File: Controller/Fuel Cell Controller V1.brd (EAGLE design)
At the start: 160 x 100 mm, 131 parts, among them IC1 4081D, M1 MOSFETBOARD, T1 TEENSY_3.1_ALL_PINS, U1 SN74ALS153D, U2 MAX3221CPWR, U3 ATMEGA328P_TQFP, U4 ATMEGA328P_TQFP, U5 MAX3221CPWR, U6 ATMEGA328P_TQFP

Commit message: added gerbers
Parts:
- removed U$1: TRUMP, trump:TRUMP
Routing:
- net SDA: track 242.7 -> 241.0 mm
- net SCL: track 237.0 -> 236.1 mm
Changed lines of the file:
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@@
 <setting verticaltext="up"/>
 </settings>
-<grid distance="0.003125" unitdist="inch" unit="inch" style="lines" multiple="1" display="no" altdistance="0.025" altunitdist="inch" altunit="inch"/>
+<grid distance="0.003125" unitdist="inch" unit="mil" style="lines" multiple="1" display="no" altdistance="0.025" altunitdist="inch" altunit="inch"/>
 <layers>
 <layer number="1" name="Top" color="4" fill="1" visible="yes" active="yes"/>
@@
 <attribute name="VALUE" x="80.0735" y="91.424125" size="0.7" layer="22" ratio="15" rot="MR180"/>
 </element>
-<element name="U$1" library="trump" package="TRUMP" value="TRUMP" x="148.11375" y="64.849375" rot="MR0"/>
 </elements>
 <signals>
@@
 <wire x1="67.31" y1="70.485" x2="67.31" y2="72.39" width="0.4064" layer="16"/>
 <via x="67.31" y="72.39" extent="1-16" drill="0.6"/>
-<wire x1="78.74" y1="52.07" x2="81.28" y2="49.53" width="0.4064" layer="1"/>
-<wire x1="81.28" y1="49.53" x2="138.1125" y2="49.53" width="0.4064" layer="1"/>
-<wire x1="138.1125" y1="49.53" x2="152.7175" y2="34.925" width="0.4064" layer="1"/>
-<wire x1="152.7175" y1="34.925" x2="152.7175" y2="32.0675" width="0.4064" layer="1"/>
-<wire x1="152.7175" y1="32.0675" x2="156.845" y2="27.94" width="0.4064" layer="1"/>
+<wire x1="78.74" y1="52.07" x2="81.12125" y2="49.68875" width="0.4064" layer="1"/>
+<wire x1="81.12125" y1="49.68875" x2="81.28" y2="49.53" width="0.4064" layer="1"/>
 <wire x1="40.1574" y1="36.76" x2="38.805" y2="36.76" width="0.4064" layer="1"/>
 <wire x1="38.805" y1="36.76" x2="37.4253125" y2="38.1396875" width="0.4064" layer="1"/>
@@
 <wire x1="37.62375" y1="38.735" x2="37.62375" y2="38.338125" width="0.4064" layer="1"/>
 <wire x1="37.62375" y1="38.338125" x2="37.4253125" y2="38.1396875" width="0.4064" layer="1"/>
+<wire x1="156.845" y1="27.94" x2="149.86" y2="27.94" width="0.4064" layer="1"/>
+<wire x1="149.86" y1="27.94" x2="128.349375" y2="49.450625" width="0.4064" layer="1"/>
+<wire x1="128.349375" y1="49.450625" x2="81.359375" y2="49.450625" width="0.4064" layer="1"/>
+<wire x1="81.359375" y1="49.450625" x2="81.28" y2="49.53" width="0.4064" layer="1"/>
 </signal>
 <signal name="SCL">
@@
 <wire x1="68.58" y1="65.405" x2="68.58" y2="71.4375" width="0.4064" layer="1"/>
 <wire x1="81.28" y1="52.07" x2="82.8675" y2="50.4825" width="0.4064" layer="1"/>
-<wire x1="82.8675" y1="50.4825" x2="138.43" y2="50.4825" width="0.4064" layer="1"/>
-<wire x1="138.43" y1="50.4825" x2="153.67" y2="35.2425" width="0.4064" layer="1"/>
-<wire x1="153.67" y1="35.2425" x2="153.67" y2="33.655" width="0.4064" layer="1"/>
-<wire x1="153.67" y1="33.655" x2="156.845" y2="30.48" width="0.4064" layer="1"/>
 <wire x1="40.1574" y1="35.96" x2="38.6525" y2="35.96" width="0.4064" layer="1"/>
 <wire x1="38.6525" y1="35.96" x2="37.7428125" y2="36.8696875" width="0.4064" layer="1"/>
@@
 <wire x1="37.62375" y1="30.00375" x2="37.62375" y2="36.750625" width="0.4064" layer="1"/>
 <wire x1="37.62375" y1="36.750625" x2="37.7428125" y2="36.8696875" width="0.4064" layer="1"/>
+<wire x1="82.8675" y1="50.4825" x2="131.365625" y2="50.4825" width="0.4064" layer="1"/>
+<wire x1="131.365625" y1="50.4825" x2="150.891875" y2="30.95625" width="0.4064" layer="1"/>
+<wire x1="150.891875" y1="30.95625" x2="156.36875" y2="30.95625" width="0.4064" layer="1"/>
+<wire x1="156.36875" y1="30.95625" x2="156.845" y2="30.48" width="0.4064" layer="1"/>
 </signal>
 <signal name="+3.3V">
@@
 <wire x1="32.7025" y1="28.865625" x2="34.051875" y2="28.865625" width="0.4064" layer="1"/>
 <wire x1="34.051875" y1="28.865625" x2="34.528125" y2="29.341875" width="0.4064" layer="1"/>
-<via x="25.24125" y="29.5275" extent="1-16" drill="0.6"/>
+<via x="25.24125" y="29.5275" extent="1-16" drill="0.5"/>
 <via x="25.55875" y="24.13" extent="1-16" drill="0.6"/>
 <via x="34.29" y="26.114375" extent="1-16" drill="0.6"/>
@@
 <wire x1="40.9575" y1="86.51875" x2="40.9575" y2="85.88375" width="1.27" layer="16"/>
 <wire x1="40.9575" y1="85.88375" x2="42.465625" y2="84.375625" width="1.778" layer="16"/>
-<wire x1="42.465625" y1="84.375625" x2="50.64125" y2="84.375625" width="1.778" layer="16"/>
-<wire x1="50.64125" y1="84.375625" x2="55.006875" y2="80.01" width="1.778" layer="16"/>
-<wire x1="55.006875" y1="80.01" x2="55.006875" y2="63.97625" width="1.778" layer="16"/>
-<wire x1="55.006875" y1="63.97625" x2="70.246875" y2="48.73625" width="1.778" layer="16"/>
-<wire x1="70.246875" y1="48.73625" x2="97.710625" y2="48.73625" width="1.778" layer="16"/>
-<wire x1="97.710625" y1="48.73625" x2="107.15625" y2="39.290625" width="1.778" layer="16"/>
+<wire x1="42.465625" y1="84.375625" x2="50.64125" y2="84.375625" width="2.1844" layer="16"/>
+<wire x1="50.64125" y1="84.375625" x2="55.006875" y2="80.01" width="2.1844" layer="16"/>
+<wire x1="55.006875" y1="80.01" x2="55.006875" y2="63.97625" width="2.1844" layer="16"/>
+<wire x1="55.006875" y1="63.97625" x2="70.246875" y2="48.73625" width="2.1844" layer="16"/>
+<wire x1="70.246875" y1="48.73625" x2="97.710625" y2="48.73625" width="2.1844" layer="16"/>
+<wire x1="97.710625" y1="48.73625" x2="107.15625" y2="39.290625" width="2.1844" layer="16"/>
 <polygon width="0.4064" layer="1" rank="2">
 <vertex x="75.565" y="-0.15875"/>
@@
 <vertex x="75.485625" y="11.7475"/>
 </polygon>
-<wire x1="107.15625" y1="39.290625" x2="107.15625" y2="32.146875" width="1.778" layer="16"/>
-<wire x1="107.15625" y1="30.1625" x2="107.15625" y2="3.33375" width="1.778" layer="16"/>
-<wire x1="107.15625" y1="3.33375" x2="107.076875" y2="3.254375" width="1.778" layer="16"/>
+<wire x1="107.15625" y1="39.290625" x2="107.15625" y2="32.146875" width="2.1844" layer="16"/>
+<wire x1="107.394375" y1="30.1625" x2="107.394375" y2="3.33375" width="2.1844" layer="16"/>
+<wire x1="107.394375" y1="3.33375" x2="107.076875" y2="3.254375" width="1.778" layer="16"/>
 <via x="107.076875" y="3.254375" extent="1-16" drill="0.6" shape="square"/>
-<wire x1="107.076875" y1="3.254375" x2="107.076875" y2="2.619375" width="1.778" layer="1"/>
-<wire x1="107.076875" y1="2.619375" x2="106.441875" y2="1.984375" width="1.778" layer="1"/>
+<wire x1="107.076875" y1="3.254375" x2="107.076875" y2="2.619375" width="2.1844" layer="1"/>
+<wire x1="107.076875" y1="2.619375" x2="106.441875" y2="1.984375" width="2.1844" layer="1"/>
 <wire x1="105.43875" y1="25.638125" x2="105.43875" y2="28.445" width="1.778" layer="1"/>
-<wire x1="105.43875" y1="28.445" x2="107.15625" y2="30.1625" width="1.778" layer="1"/>
-<via x="107.15625" y="30.1625" extent="1-16" drill="0.6" shape="square"/>
-<wire x1="107.15625" y1="30.1625" x2="107.15625" y2="32.146875" width="1.778" layer="16"/>
+<wire x1="105.43875" y1="28.445" x2="107.394375" y2="30.1625" width="1.778" layer="1"/>
+<via x="107.394375" y="30.1625" extent="1-16" drill="0.6" shape="square"/>
+<wire x1="107.394375" y1="30.1625" x2="107.15625" y2="32.146875" width="2.1844" layer="16"/>
 </signal>
 <signal name="FCC_R">

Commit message: couple board revisions
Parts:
- added U$1: TRUMP, trump:TRUMP
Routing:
- net SDA: track 241.0 -> 242.7 mm
- net SCL: track 236.1 -> 237.0 mm
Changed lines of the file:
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@@
 <setting verticaltext="up"/>
 </settings>
-<grid distance="0.003125" unitdist="inch" unit="mil" style="lines" multiple="1" display="no" altdistance="0.025" altunitdist="inch" altunit="inch"/>
+<grid distance="0.003125" unitdist="inch" unit="inch" style="lines" multiple="1" display="no" altdistance="0.025" altunitdist="inch" altunit="inch"/>
 <layers>
 <layer number="1" name="Top" color="4" fill="1" visible="yes" active="yes"/>
@@
 <attribute name="VALUE" x="80.0735" y="91.424125" size="0.7" layer="22" ratio="15" rot="MR180"/>
 </element>
+<element name="U$1" library="trump" package="TRUMP" value="TRUMP" x="148.11375" y="64.849375" rot="MR0"/>
 </elements>
 <signals>
@@
 <wire x1="67.31" y1="70.485" x2="67.31" y2="72.39" width="0.4064" layer="16"/>
 <via x="67.31" y="72.39" extent="1-16" drill="0.6"/>
-<wire x1="78.74" y1="52.07" x2="81.12125" y2="49.68875" width="0.4064" layer="1"/>
-<wire x1="81.12125" y1="49.68875" x2="81.28" y2="49.53" width="0.4064" layer="1"/>
+<wire x1="78.74" y1="52.07" x2="81.28" y2="49.53" width="0.4064" layer="1"/>
+<wire x1="81.28" y1="49.53" x2="138.1125" y2="49.53" width="0.4064" layer="1"/>
+<wire x1="138.1125" y1="49.53" x2="152.7175" y2="34.925" width="0.4064" layer="1"/>
+<wire x1="152.7175" y1="34.925" x2="152.7175" y2="32.0675" width="0.4064" layer="1"/>
+<wire x1="152.7175" y1="32.0675" x2="156.845" y2="27.94" width="0.4064" layer="1"/>
 <wire x1="40.1574" y1="36.76" x2="38.805" y2="36.76" width="0.4064" layer="1"/>
 <wire x1="38.805" y1="36.76" x2="37.4253125" y2="38.1396875" width="0.4064" layer="1"/>
@@
 <wire x1="37.62375" y1="38.735" x2="37.62375" y2="38.338125" width="0.4064" layer="1"/>
 <wire x1="37.62375" y1="38.338125" x2="37.4253125" y2="38.1396875" width="0.4064" layer="1"/>
-<wire x1="156.845" y1="27.94" x2="149.86" y2="27.94" width="0.4064" layer="1"/>
-<wire x1="149.86" y1="27.94" x2="128.349375" y2="49.450625" width="0.4064" layer="1"/>
-<wire x1="128.349375" y1="49.450625" x2="81.359375" y2="49.450625" width="0.4064" layer="1"/>
-<wire x1="81.359375" y1="49.450625" x2="81.28" y2="49.53" width="0.4064" layer="1"/>
 </signal>
 <signal name="SCL">
@@
 <wire x1="68.58" y1="65.405" x2="68.58" y2="71.4375" width="0.4064" layer="1"/>
 <wire x1="81.28" y1="52.07" x2="82.8675" y2="50.4825" width="0.4064" layer="1"/>
+<wire x1="82.8675" y1="50.4825" x2="138.43" y2="50.4825" width="0.4064" layer="1"/>
+<wire x1="138.43" y1="50.4825" x2="153.67" y2="35.2425" width="0.4064" layer="1"/>
+<wire x1="153.67" y1="35.2425" x2="153.67" y2="33.655" width="0.4064" layer="1"/>
+<wire x1="153.67" y1="33.655" x2="156.845" y2="30.48" width="0.4064" layer="1"/>
 <wire x1="40.1574" y1="35.96" x2="38.6525" y2="35.96" width="0.4064" layer="1"/>
 <wire x1="38.6525" y1="35.96" x2="37.7428125" y2="36.8696875" width="0.4064" layer="1"/>
@@
 <wire x1="37.62375" y1="30.00375" x2="37.62375" y2="36.750625" width="0.4064" layer="1"/>
 <wire x1="37.62375" y1="36.750625" x2="37.7428125" y2="36.8696875" width="0.4064" layer="1"/>
-<wire x1="82.8675" y1="50.4825" x2="131.365625" y2="50.4825" width="0.4064" layer="1"/>
-<wire x1="131.365625" y1="50.4825" x2="150.891875" y2="30.95625" width="0.4064" layer="1"/>
-<wire x1="150.891875" y1="30.95625" x2="156.36875" y2="30.95625" width="0.4064" layer="1"/>
-<wire x1="156.36875" y1="30.95625" x2="156.845" y2="30.48" width="0.4064" layer="1"/>
 </signal>
 <signal name="+3.3V">
@@
 <wire x1="32.7025" y1="28.865625" x2="34.051875" y2="28.865625" width="0.4064" layer="1"/>
 <wire x1="34.051875" y1="28.865625" x2="34.528125" y2="29.341875" width="0.4064" layer="1"/>
-<via x="25.24125" y="29.5275" extent="1-16" drill="0.5"/>
+<via x="25.24125" y="29.5275" extent="1-16" drill="0.6"/>
 <via x="25.55875" y="24.13" extent="1-16" drill="0.6"/>
 <via x="34.29" y="26.114375" extent="1-16" drill="0.6"/>
@@
 <wire x1="40.9575" y1="86.51875" x2="40.9575" y2="85.88375" width="1.27" layer="16"/>
 <wire x1="40.9575" y1="85.88375" x2="42.465625" y2="84.375625" width="1.778" layer="16"/>
-<wire x1="42.465625" y1="84.375625" x2="50.64125" y2="84.375625" width="2.1844" layer="16"/>
-<wire x1="50.64125" y1="84.375625" x2="55.006875" y2="80.01" width="2.1844" layer="16"/>
-<wire x1="55.006875" y1="80.01" x2="55.006875" y2="63.97625" width="2.1844" layer="16"/>
-<wire x1="55.006875" y1="63.97625" x2="70.246875" y2="48.73625" width="2.1844" layer="16"/>
-<wire x1="70.246875" y1="48.73625" x2="97.710625" y2="48.73625" width="2.1844" layer="16"/>
-<wire x1="97.710625" y1="48.73625" x2="107.15625" y2="39.290625" width="2.1844" layer="16"/>
+<wire x1="42.465625" y1="84.375625" x2="50.64125" y2="84.375625" width="1.778" layer="16"/>
+<wire x1="50.64125" y1="84.375625" x2="55.006875" y2="80.01" width="1.778" layer="16"/>
+<wire x1="55.006875" y1="80.01" x2="55.006875" y2="63.97625" width="1.778" layer="16"/>
+<wire x1="55.006875" y1="63.97625" x2="70.246875" y2="48.73625" width="1.778" layer="16"/>
+<wire x1="70.246875" y1="48.73625" x2="97.710625" y2="48.73625" width="1.778" layer="16"/>
+<wire x1="97.710625" y1="48.73625" x2="107.15625" y2="39.290625" width="1.778" layer="16"/>
 <polygon width="0.4064" layer="1" rank="2">
 <vertex x="75.565" y="-0.15875"/>
@@
 <vertex x="75.485625" y="11.7475"/>
 </polygon>
-<wire x1="107.15625" y1="39.290625" x2="107.15625" y2="32.146875" width="2.1844" layer="16"/>
-<wire x1="107.394375" y1="30.1625" x2="107.394375" y2="3.33375" width="2.1844" layer="16"/>
-<wire x1="107.394375" y1="3.33375" x2="107.076875" y2="3.254375" width="1.778" layer="16"/>
+<wire x1="107.15625" y1="39.290625" x2="107.15625" y2="32.146875" width="1.778" layer="16"/>
+<wire x1="107.15625" y1="30.1625" x2="107.15625" y2="3.33375" width="1.778" layer="16"/>
+<wire x1="107.15625" y1="3.33375" x2="107.076875" y2="3.254375" width="1.778" layer="16"/>
 <via x="107.076875" y="3.254375" extent="1-16" drill="0.6" shape="square"/>
-<wire x1="107.076875" y1="3.254375" x2="107.076875" y2="2.619375" width="2.1844" layer="1"/>
-<wire x1="107.076875" y1="2.619375" x2="106.441875" y2="1.984375" width="2.1844" layer="1"/>
+<wire x1="107.076875" y1="3.254375" x2="107.076875" y2="2.619375" width="1.778" layer="1"/>
+<wire x1="107.076875" y1="2.619375" x2="106.441875" y2="1.984375" width="1.778" layer="1"/>
 <wire x1="105.43875" y1="25.638125" x2="105.43875" y2="28.445" width="1.778" layer="1"/>
-<wire x1="105.43875" y1="28.445" x2="107.394375" y2="30.1625" width="1.778" layer="1"/>
-<via x="107.394375" y="30.1625" extent="1-16" drill="0.6" shape="square"/>
-<wire x1="107.394375" y1="30.1625" x2="107.15625" y2="32.146875" width="2.1844" layer="16"/>
+<wire x1="105.43875" y1="28.445" x2="107.15625" y2="30.1625" width="1.778" layer="1"/>
+<via x="107.15625" y="30.1625" extent="1-16" drill="0.6" shape="square"/>
+<wire x1="107.15625" y1="30.1625" x2="107.15625" y2="32.146875" width="1.778" layer="16"/>
 </signal>
 <signal name="FCC_R">

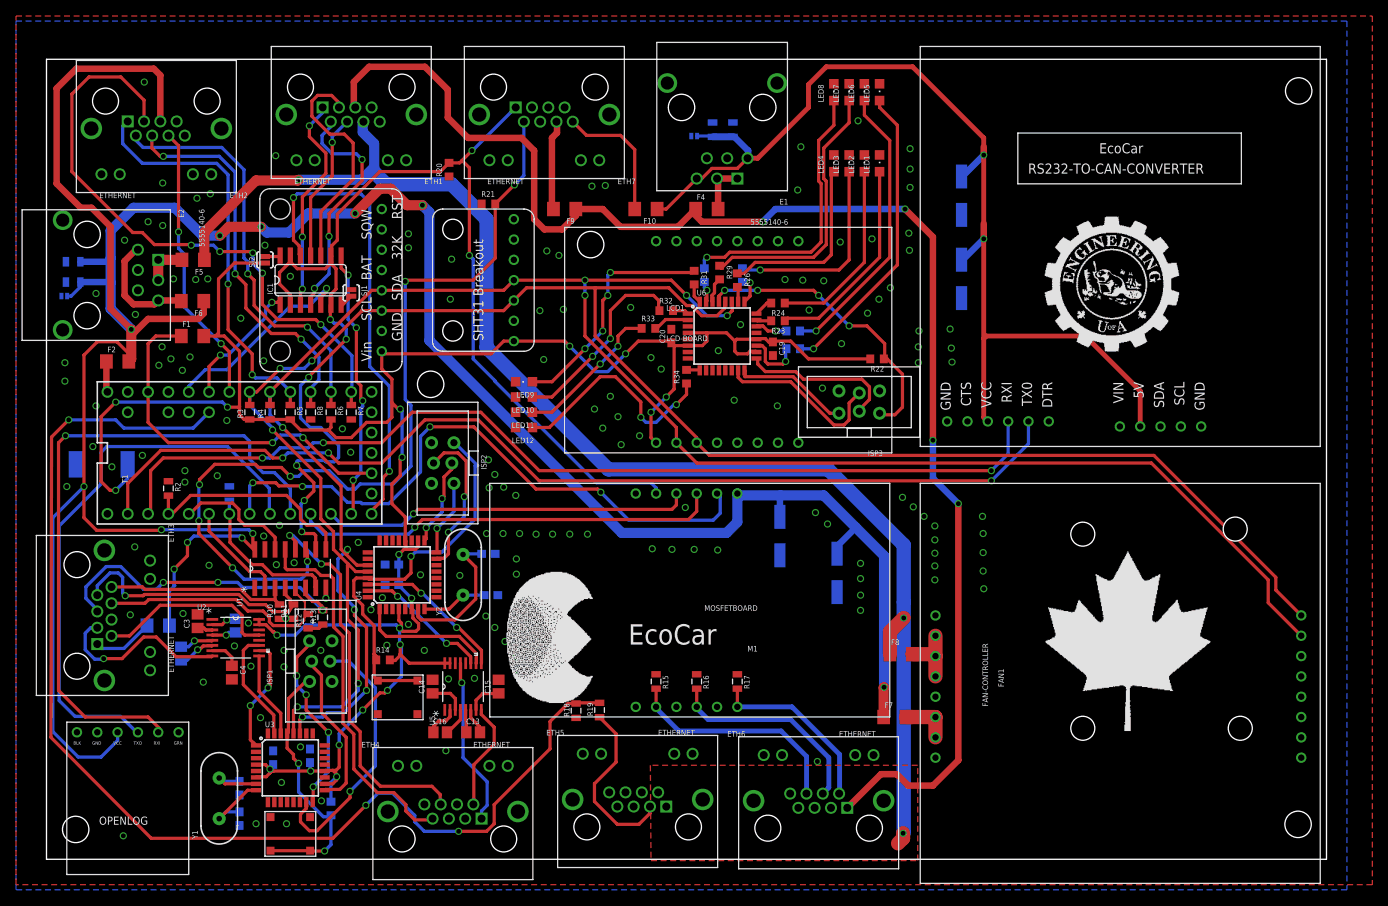
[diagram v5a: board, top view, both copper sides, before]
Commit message: cleaned up silk screens
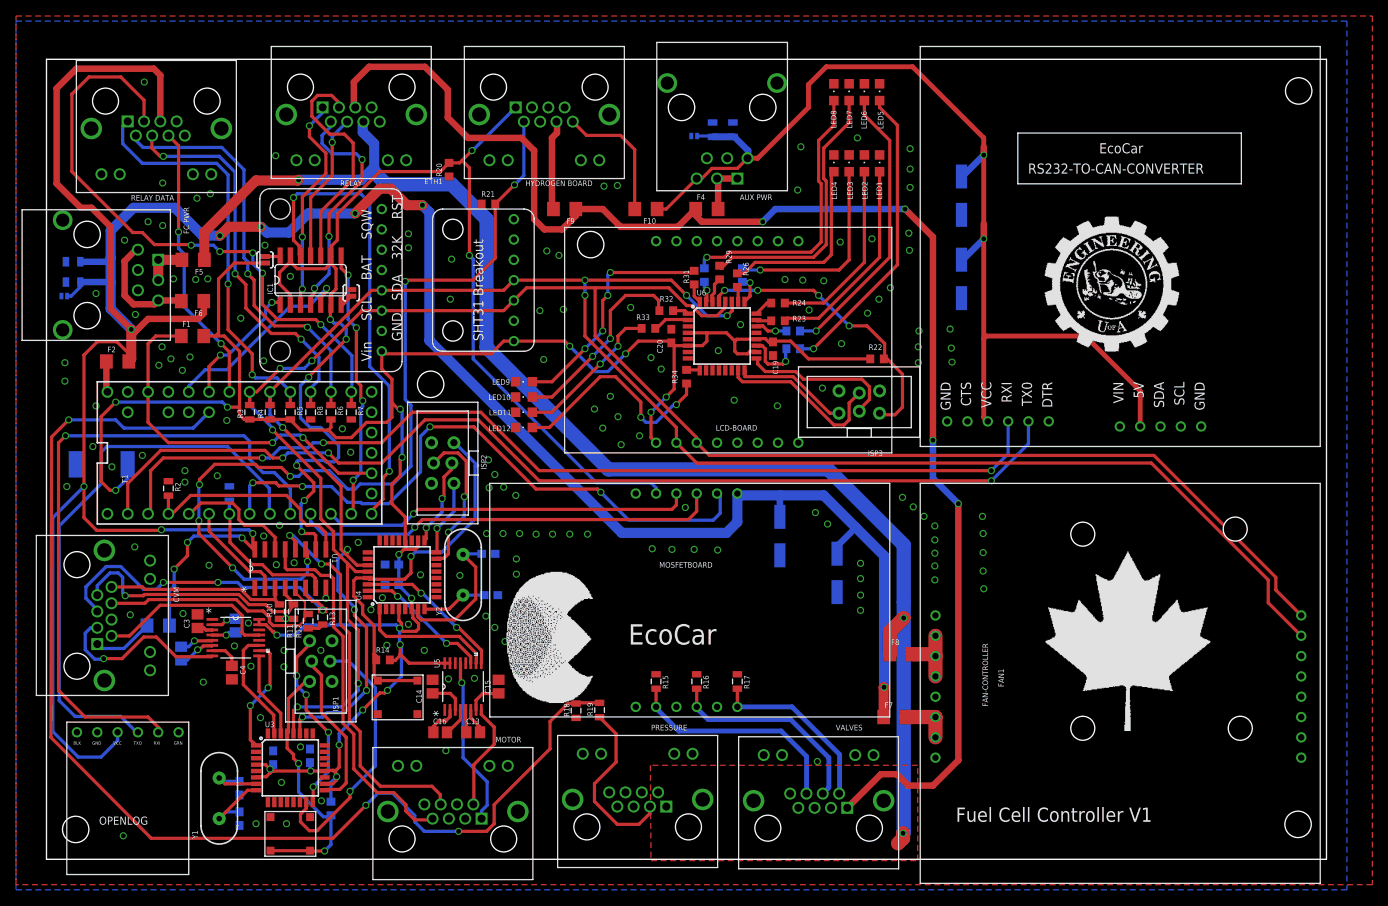
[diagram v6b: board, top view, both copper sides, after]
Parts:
- removed U$1: TRUMP, trump:TRUMP
- E1: value 5555140-6 -> AUX PWR
- E2: value 5555140-6 -> FC PWR
- ETH1: value ETHERNET -> RELAY
- ETH2: value ETHERNET -> RELAY DATA
- ETH3: value ETHERNET -> CVM
- ETH4: value ETHERNET -> MOTOR
- ETH5: value ETHERNET -> PRESSURE
- ETH6: value ETHERNET -> VALVES
- ETH7: value ETHERNET -> HYDROGEN BOARD
- moved FRAME1 2.84 mm to (0.00, 0.00)
- moved FRAME2 2.84 mm to (0.00, 0.00)
- moved FRAME3 2.84 mm to (0.00, 0.00)
- moved FRAME5 2.84 mm to (0.00, 0.00)
- moved FRAME6 2.84 mm to (0.00, 0.00)
- moved FRAME7 2.69 mm to (0.00, 0.00)
- moved FRAME4 1.27 mm to (0.00, 0.00)
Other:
- board text added: "Fuel Cell Controller V1"
